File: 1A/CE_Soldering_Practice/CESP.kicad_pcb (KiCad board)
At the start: 2 copper layers, 55.9 x 44.7 mm, 9 parts

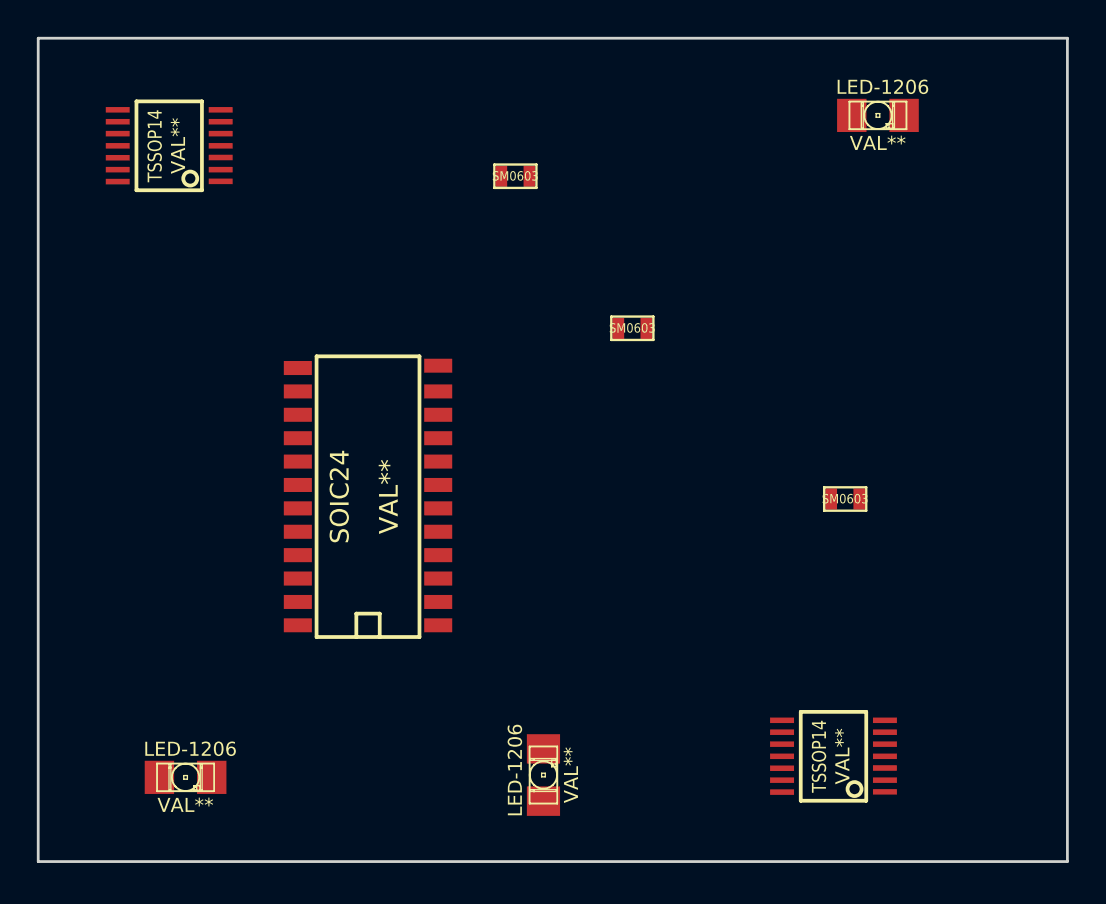
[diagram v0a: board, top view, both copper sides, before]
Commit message: My soldering practice board design
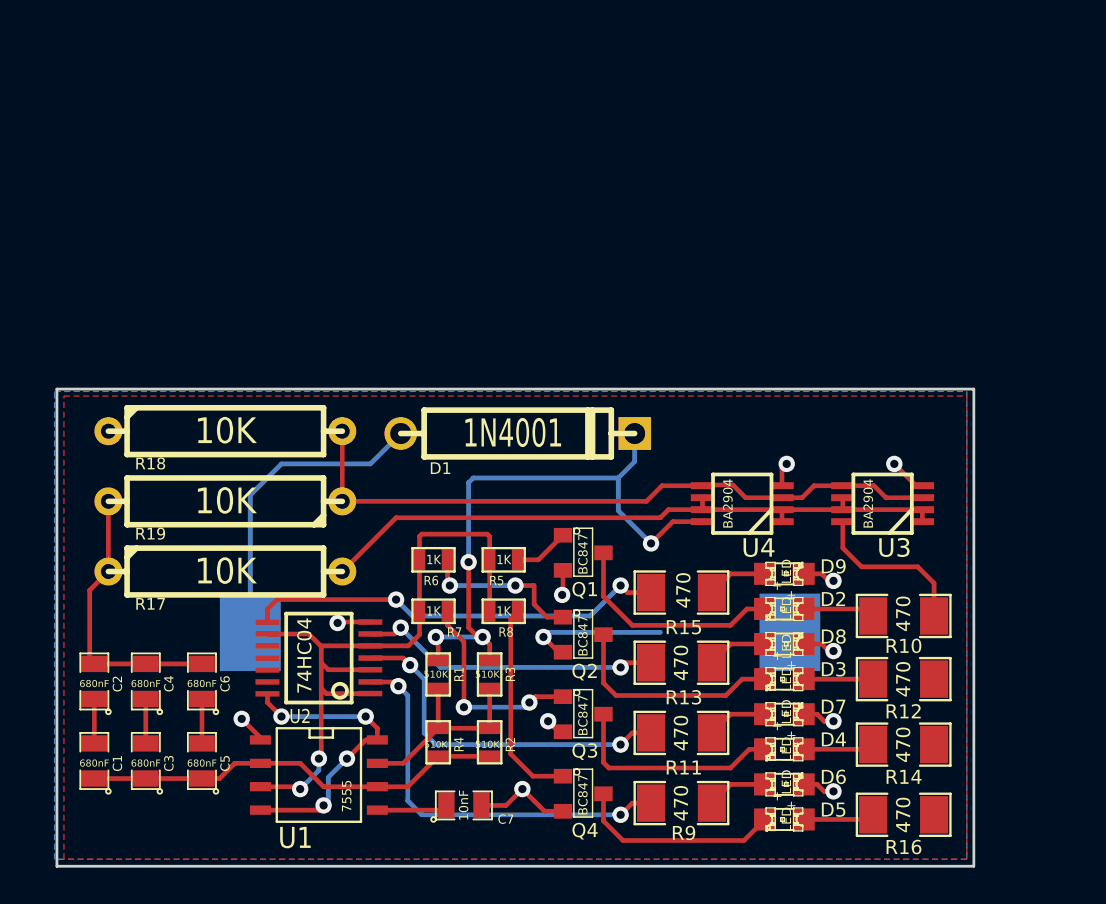
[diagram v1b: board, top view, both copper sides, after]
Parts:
- removed LED-1206 (x3): VAL**, LED-1206
- removed SM0603 (x3): Val**, SM0603
- removed SOIC24: VAL**, SOIC24
- removed TSSOP14 (x2): VAL**, TSSOP14
- added BT1: BATTERY, BU2032SM-BT-GTR, B.Cu at (182.1, 128.0)
- added C1: 680nF, SM0805, F.Cu at (159.0, 135.0)
- added C2: 680nF, SM0805, F.Cu at (159.0, 130.7)
- added C3: 680nF, SM0805, F.Cu at (161.8, 135.0)
- added C4: 680nF, SM0805, F.Cu at (161.8, 130.7)
- added C5: 680nF, SM0805, F.Cu at (164.8, 135.0)
- added C6: 680nF, SM0805, F.Cu at (164.8, 130.7)
- added C7: 10nF, SM0805, F.Cu at (179.1, 137.4)
- added D1: 1N4001, D5, F.Cu at (182.0, 117.2)
- added D2: LED, LED-0805, F.Cu at (196.5, 126.7)
- added D3: LED, LED-0805, F.Cu at (196.5, 130.6)
- added D4: LED, LED-0805, F.Cu at (196.5, 134.4)
- added D5: LED, LED-0805, F.Cu at (196.5, 138.2)
- added D6: LED, LED-0805, F.Cu at (196.5, 136.3)
- added D7: LED, LED-0805, F.Cu at (196.5, 132.5)
- added D8: LED, LED-0805, F.Cu at (196.5, 128.7)
- added D9: LED, LED-0805, F.Cu at (196.5, 124.8)
- added Q1: BC847, SOT23, F.Cu at (185.5, 123.7)
- added Q2: BC847, SOT23, F.Cu at (185.5, 128.1)
- added Q3: BC847, SOT23, F.Cu at (185.5, 132.5)
- added Q4: BC847, SOT23, F.Cu at (185.5, 136.8)
- added R1: 510K, SM0603, F.Cu at (177.7, 130.3)
- added R10: 470, SM1206, F.Cu at (202.9, 127.1)
- added R11: 470, SM1206, F.Cu at (190.9, 133.5)
- added R12: 470, SM1206, F.Cu at (202.9, 130.6)
- added R13: 470, SM1206, F.Cu at (190.9, 129.7)
- added R14: 470, SM1206, F.Cu at (202.9, 134.1)
- added R15: 470, SM1206, F.Cu at (190.9, 125.9)
- added R16: 470, SM1206, F.Cu at (202.9, 137.9)
- added R17: 10K, R5, F.Cu at (166.1, 124.7)
- added R18: 10K, R5, F.Cu at (166.1, 117.1)
- added R19: 10K, R5, F.Cu at (166.1, 120.9)
- added R2: 510K, SM0603, F.Cu at (180.5, 134.0)
- added R3: 510K, SM0603, F.Cu at (180.5, 130.3)
- added R4: 510K, SM0603, F.Cu at (177.7, 134.0)
- added R5: 1K, SM0603, F.Cu at (181.2, 124.1)
- added R6: 1K, SM0603, F.Cu at (177.4, 124.1)
- added R7: 1K, SM0603, F.Cu at (177.4, 126.9)
- added R8: 1K, SM0603, F.Cu at (181.2, 126.9)
- added R9: 470, SM1206, F.Cu at (190.9, 137.3)
- added U1: 7555, SO8N, F.Cu at (171.2, 135.8)
- added U2: 74HC04, TSSOP14, F.Cu at (171.2, 129.4)
- added U3: BA2904, MSOP_8, F.Cu at (201.8, 121.0)
- added U4: BA2904, MSOP_8, F.Cu at (194.2, 121.0)
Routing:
- net VCC: track 0.00 -> 58.0 mm, vias 0 -> 8
- net GND: track 0.00 -> 44.5 mm, vias 0 -> 12
- net N-000003: track 0.00 -> 38.2 mm, vias 0 -> 2
- net N-000002: track 0.00 -> 36.5 mm
- net N-000007: track 0.00 -> 35.5 mm
- net N-0000012: track 0.00 -> 23.0 mm
- net N-0000022: track 0.00 -> 23.0 mm, vias 0 -> 2
- net N-0000010: track 0.00 -> 21.8 mm, vias 0 -> 2
- net N-0000016: track 0.00 -> 19.2 mm, vias 0 -> 2
- net N-000006: track 0.00 -> 17.0 mm
- net N-0000019: track 0.00 -> 16.4 mm, vias 0 -> 2
- net N-0000015: track 0.00 -> 12.2 mm
- net N-0000025: track 0.00 -> 12.0 mm
- net N-0000026: track 0.00 -> 11.9 mm
- net N-000009: track 0.00 -> 11.2 mm
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- added copper zone on B.Cu, net GND
- added copper zone on F.Cu, net VCC
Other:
- board size 55.9 x 44.7 mm -> 49.8 x 25.9 mm
- board text added: "+"
- board text added: "Sam C. Jan 2014"
- board text added: "Soldering Practice"
- board text removed: "NOTE: THIS IS JUST A TEST BOARD REMOVE ALL COMPONENTS AND CREATE YOUR OWN INCLUDE SCHEMATIC HOOKUPS/NETLIST"
